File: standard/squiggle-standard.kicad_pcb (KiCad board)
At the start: 2 copper layers, 116 x 101.2 mm, 38 parts, among them SW1 switch, SW10 switch, SW11 switch, SW12 switch, SW13 switch, SW14 switch, SW15 switch, SW16 switch, SW17 switch, SW2 switch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

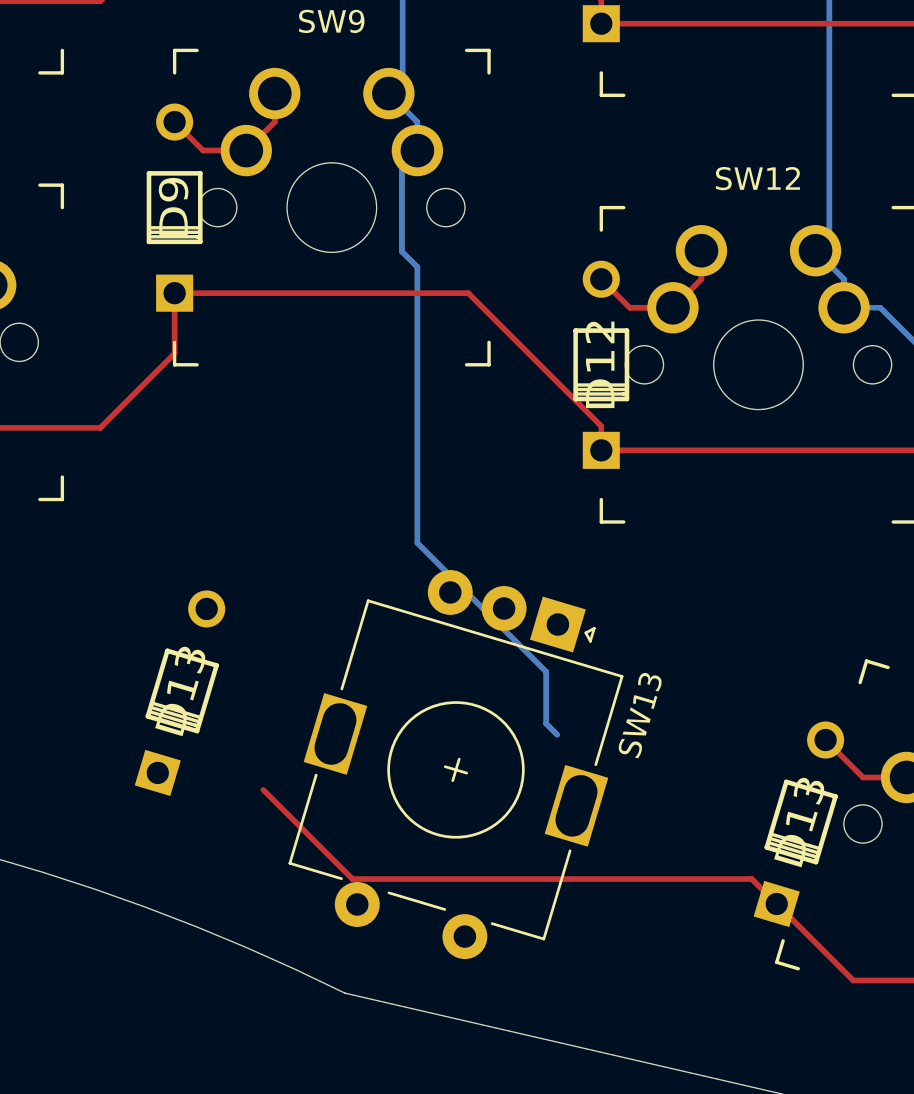
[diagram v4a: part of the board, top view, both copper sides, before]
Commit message: added encoder to schematic and wired switch pinouts
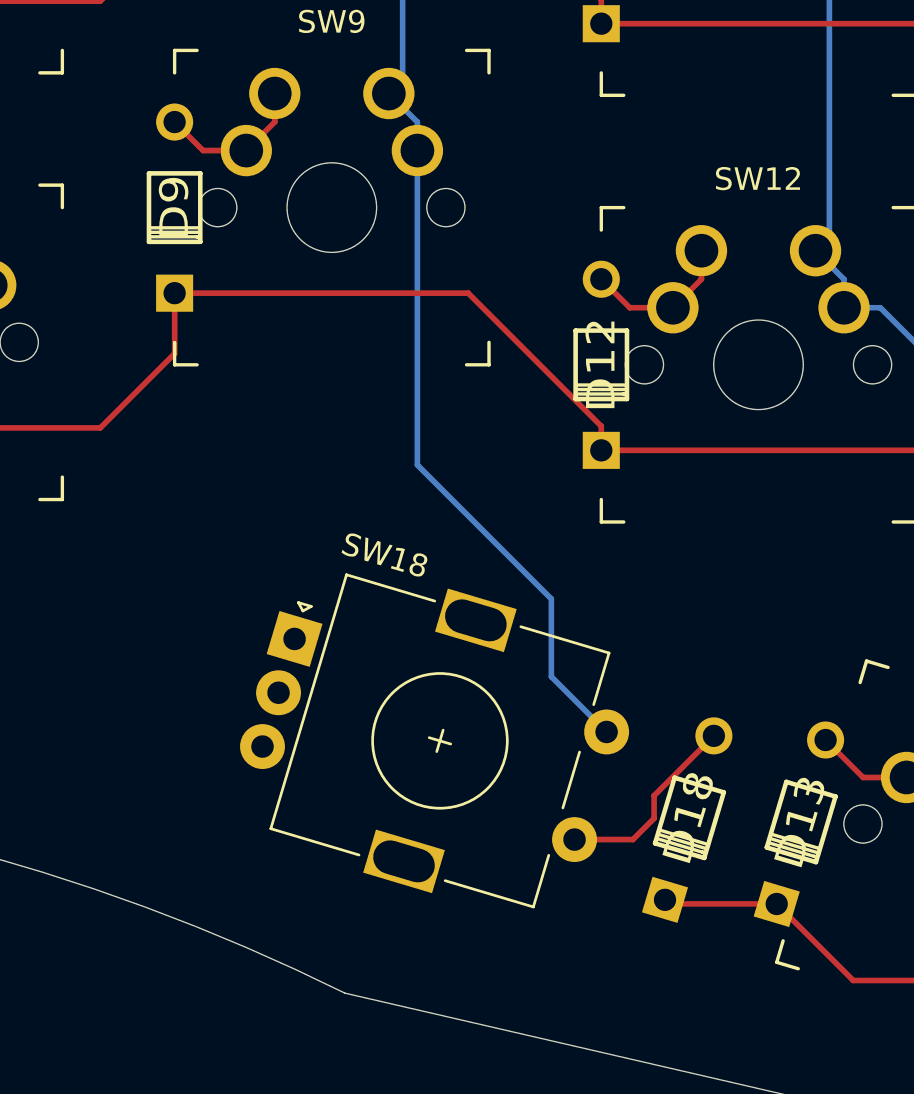
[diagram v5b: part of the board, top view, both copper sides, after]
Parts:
- moved D18 23.3 mm to (83.9, 86.2)
- moved SW18 11.7 mm to (66.3, 78.2), turned to -16.6 degrees
- renumbered D13 to D18, SW13 to SW18
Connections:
- D18 pad 2: Net-(D10-Pad2) -> (no net)
- SW18 pad S2: (no net) -> COL2
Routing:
- net ROW3: track 95.0 -> 75.1 mm
- net (no net): track 0.00 -> 8.71 mm
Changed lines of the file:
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@@
   )
   (footprint "Rotary_Encoder:RotaryEncoder_Alps_EC11E-Switch_Vertical_H20mm" (layer "F.Cu")
-    (at 78.067048 77.566382 -106.6)
+    (at 66.341382 78.207953 -16.6)
     (descr "Alps rotary encoder, EC12E... with switch, vertical shaft, http://www.alps.com/prod/info/E/HTML/Encoder/Incremental/EC11/EC11E15204A3.html")
     (tags "rotary encoder")
     (attr through_hole)
-    (fp_text reference "SW13" (at 2.8 -4.7 73.4) (layer "F.SilkS")
+    (fp_text reference "SW18" (at 2.8 -4.7 163.4) (layer "F.SilkS")
       (effects (font (size 1 1) (thickness 0.15)))
     )
-    (fp_text value "switch" (at 7.5 10.4 73.4) (layer "F.Fab")
+    (fp_text value "switch" (at 7.5 10.4 163.4) (layer "F.Fab")
       (effects (font (size 1 1) (thickness 0.15)))
     )
-    (fp_text user "2.00u" (at -15.24 8.255 73.4) (layer "Dwgs.User")
+    (fp_text user "2.00u" (at -15.24 8.255 163.4) (layer "Dwgs.User")
       (effects (font (size 1.524 1.524) (thickness 0.3048)))
     )
-    (fp_text user "${VALUE}" (at 0 8.255 73.4) (layer "B.Fab")
+    (fp_text user "${VALUE}" (at 0 8.255 163.4) (layer "B.Fab")
       (effects (font (size 1 1) (thickness 0.15)) (justify mirror))
     )
-    (fp_text user "${REFERENCE}" (at 11.1 6.3 73.4) (layer "F.Fab")
+    (fp_text user "${REFERENCE}" (at 11.1 6.3 163.4) (layer "F.Fab")
       (effects (font (size 1 1) (thickness 0.15)))
     )
@@
     (fp_line (start 13.5 -3.3) (end 13.5 8.3) (layer "F.Fab") (width 0.12))
     (fp_circle (center 7.5 2.5) (end 10.5 2.5) (layer "F.Fab") (width 0.12) (fill none))
-    (pad "A" thru_hole rect (at 0 0 253.4) (size 2 2) (drill 1) (layers *.Cu *.Mask))
-    (pad "B" thru_hole circle (at 0 5 253.4) (size 2 2) (drill 1) (layers *.Cu *.Mask))
-    (pad "C" thru_hole circle (at 0 2.5 253.4) (size 2 2) (drill 1) (layers *.Cu *.Mask))
-    (pad "MP" thru_hole rect (at 7.5 -3.1 253.4) (size 3.2 2) (drill oval 2.8 1.5) (layers *.Cu *.Mask))
-    (pad "MP" thru_hole rect (at 7.5 8.1 253.4) (size 3.2 2) (drill oval 2.8 1.5) (layers *.Cu *.Mask))
-    (pad "S1" thru_hole circle (at 14.5 5 253.4) (size 2 2) (drill 1) (layers *.Cu *.Mask))
-    (pad "S2" thru_hole circle (at 14.5 0 253.4) (size 2 2) (drill 1) (layers *.Cu *.Mask))
+    (pad "A" thru_hole rect (at 0 0 343.4) (size 2 2) (drill 1) (layers *.Cu *.Mask))
+    (pad "B" thru_hole circle (at 0 5 343.4) (size 2 2) (drill 1) (layers *.Cu *.Mask))
+    (pad "GND" thru_hole circle (at 0 2.5 343.4) (size 2 2) (drill 1) (layers *.Cu *.Mask))
+    (pad "MP" thru_hole rect (at 7.5 -3.1 343.4) (size 3.2 2) (drill oval 2.8 1.5) (layers *.Cu *.Mask))
+    (pad "MP" thru_hole rect (at 7.5 8.1 343.4) (size 3.2 2) (drill oval 2.8 1.5) (layers *.Cu *.Mask))
+    (pad "S1" thru_hole circle (at 14.5 5 343.4) (size 2 2) (drill 1) (layers *.Cu *.Mask))
+    (pad "S2" thru_hole circle (at 14.5 0 343.4) (size 2 2) (drill 1) (layers *.Cu *.Mask)
+      (net 18 "COL2"))
     (model "${KICAD6_3DMODEL_DIR}/Rotary_Encoder.3dshapes/RotaryEncoder_Alps_EC11E-Switch_Vertical_H20mm.wrl"
       (offset (xyz 0 0 0))
@@
   )
   (footprint "footprints:diode" (layer "F.Cu")
-    (at 61.338473 80.523791 -106.6)
+    (at 83.925 86.175 -106.6)
     (attr through_hole)
-    (fp_text reference "D13" (at 0 0 73.4) (layer "F.SilkS")
+    (fp_text reference "D18" (at 0 0 73.4) (layer "F.SilkS")
       (effects (font (size 1.27 1.524) (thickness 0.2032)))
     )
@@
     (pad "1" thru_hole rect locked (at 3.81 0 253.4) (size 1.651 1.651) (drill 0.9906) (layers *.Cu *.SilkS *.Mask)
       (net 15 "ROW3"))
-    (pad "2" thru_hole circle locked (at -3.81 0 253.4) (size 1.651 1.651) (drill 0.9906) (layers *.Cu *.SilkS *.Mask)
-      (net 8 "Net-(D10-Pad2)"))
+    (pad "2" thru_hole circle locked (at -3.81 0 253.4) (size 1.651 1.651) (drill 0.9906) (layers *.Cu *.SilkS *.Mask))
   )
   (footprint "footprints:trrs" (layer "B.Cu")
@@
   (gr_arc (start 135 21) (mid 135.707107 21.292893) (end 136 22) (layer "Edge.Cuts") (width 0.05))
   (gr_arc (start 124.46 111.76) (mid 123.19 112.105074) (end 121.92 111.76) (layer "Edge.Cuts") (width 0.05))
+  (segment (start 82.35 85.187264) (end 82.35 86.2) (width 0.25) (layer "F.Cu") (net 0))
+  (segment (start 82.35 86.2) (end 81.407953 87.142047) (width 0.25) (layer "F.Cu") (net 0))
+  (segment (start 85.013473 82.523791) (end 82.35 85.187264) (width 0.25) (layer "F.Cu") (net 0))
+  (segment (start 81.407953 87.142047) (end 78.808617 87.142047) (width 0.25) (layer "F.Cu") (net 0))
   (segment (start 27.46 35.19) (end 27.46 33.92) (width 0.25) (layer "F.Cu") (net 1))
   (segment (start 26.19 36.46) (end 27.46 35.19) (width 0.25) (layer "F.Cu") (net 1))
@@
   (segment (start 99 52.81) (end 113.37 52.81) (width 0.25) (layer "F.Cu") (net 14))
   (segment (start 61 46.5) (end 61 43.81) (width 0.25) (layer "F.Cu") (net 14))
-  (segment (start 87.811527 90.011209) (end 86.700318 88.9) (width 0.25) (layer "F.Cu") (net 15))
-  (segment (start 68.920318 88.9) (end 64.951527 84.931209) (width 0.25) (layer "F.Cu") (net 15))
   (segment (start 106.68 86.36) (end 111.76 81.28) (width 0.25) (layer "F.Cu") (net 15))
   (segment (start 108.131527 93.417937) (end 106.68 91.96641) (width 0.25) (layer "F.Cu") (net 15))
+  (segment (start 83.021527 90.011209) (end 82.836527 89.826209) (width 0.25) (layer "F.Cu") (net 15))
   (segment (start 87.811527 90.011209) (end 91.218255 93.417937) (width 0.25) (layer "F.Cu") (net 15))
   (segment (start 106.68 91.96641) (end 106.68 86.36) (width 0.25) (layer "F.Cu") (net 15))
   (segment (start 91.218255 93.417937) (end 108.131527 93.417937) (width 0.25) (layer "F.Cu") (net 15))
   (segment (start 116.84 54.42) (end 117.92 53.34) (width 0.25) (layer "F.Cu") (net 15))
-  (segment (start 86.700318 88.9) (end 68.920318 88.9) (width 0.25) (layer "F.Cu") (net 15))
+  (segment (start 87.811527 90.011209) (end 83.021527 90.011209) (width 0.25) (layer "F.Cu") (net 15))
   (segment (start 111.76 81.28) (end 116.84 81.28) (width 0.25) (layer "F.Cu") (net 15))
   (segment (start 116.84 81.28) (end 116.84 54.42) (width 0.25) (layer "F.Cu") (net 15))
@@
   (segment (start 130.870022 27.920022) (end 125.79999 22.84999) (width 0.25) (layer "B.Cu") (net 18))
   (segment (start 130.870022 45.970022) (end 130.870022 27.920022) (width 0.25) (layer "B.Cu") (net 18))
+  (segment (start 80.237059 82.350434) (end 77.775 79.888375) (width 0.25) (layer "B.Cu") (net 18))
   (segment (start 78.6 20.6) (end 74.21 16.21) (width 0.25) (layer "B.Cu") (net 18))
   (segment (start 108.7864 21.84999) (end 91.34999 21.84999) (width 0.25) (layer "B.Cu") (net 18))
-  (segment (start 71.12 60.96) (end 71.12 55.88) (width 0.25) (layer "B.Cu") (net 18))
+  (segment (start 77.775 79.888375) (end 77.775 76.425) (width 0.25) (layer "B.Cu") (net 18))
   (segment (start 74.21 16.21) (end 70.52 16.21) (width 0.25) (layer "B.Cu") (net 18))
-  (segment (start 71.81 73.941934) (end 77.545436 79.67737) (width 0.25) (layer "B.Cu") (net 18))
   (segment (start 70.54 17.19) (end 70.54 15.92) (width 0.25) (layer "B.Cu") (net 18))
-  (segment (start 71.81 61.65) (end 71.81 73.941934) (width 0.25) (layer "B.Cu") (net 18))
+  (segment (start 71.81 70.46) (end 71.81 56.46) (width 0.25) (layer "B.Cu") (net 18))
   (segment (start 71.81 55.19) (end 71.81 56.46) (width 0.25) (layer "B.Cu") (net 18))
-  (segment (start 71.12 60.96) (end 71.81 61.65) (width 0.25) (layer "B.Cu") (net 18))
   (segment (start 71.155 34.575) (end 70.52 35.21) (width 0.25) (layer "B.Cu") (net 18))
   (segment (start 90.1 20.6) (end 78.6 20.6) (width 0.25) (layer "B.Cu") (net 18))
   (segment (start 71.155 36.73) (end 71.155 53.575) (width 0.25) (layer "B.Cu") (net 18))
-  (segment (start 77.545436 79.67737) (end 77.545436 81.982912) (width 0.25) (layer "B.Cu") (net 18))
+  (segment (start 77.775 76.425) (end 71.81 70.46) (width 0.25) (layer "B.Cu") (net 18))
   (segment (start 71.81 18.46) (end 70.54 17.19) (width 0.25) (layer "B.Cu") (net 18))
-  (segment (start 77.545436 81.982912) (end 78.036857 82.474333) (width 0.25) (layer "B.Cu") (net 18))
   (segment (start 91.34999 21.84999) (end 90.1 20.6) (width 0.25) (layer "B.Cu") (net 18))
   (segment (start 133.16 48.26) (end 130.870022 45.970022) (width 0.25) (layer "B.Cu") (net 18))
